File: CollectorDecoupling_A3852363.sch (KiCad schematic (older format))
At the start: 0 parts

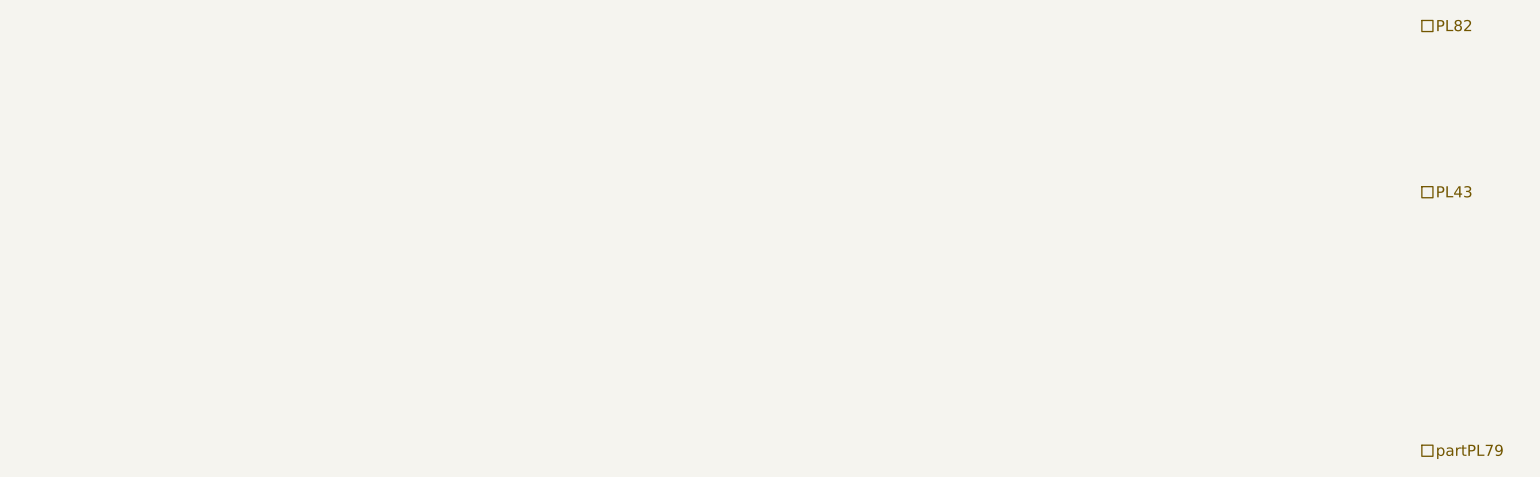
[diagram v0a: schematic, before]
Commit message: Adds Collector Decoupling (potted)
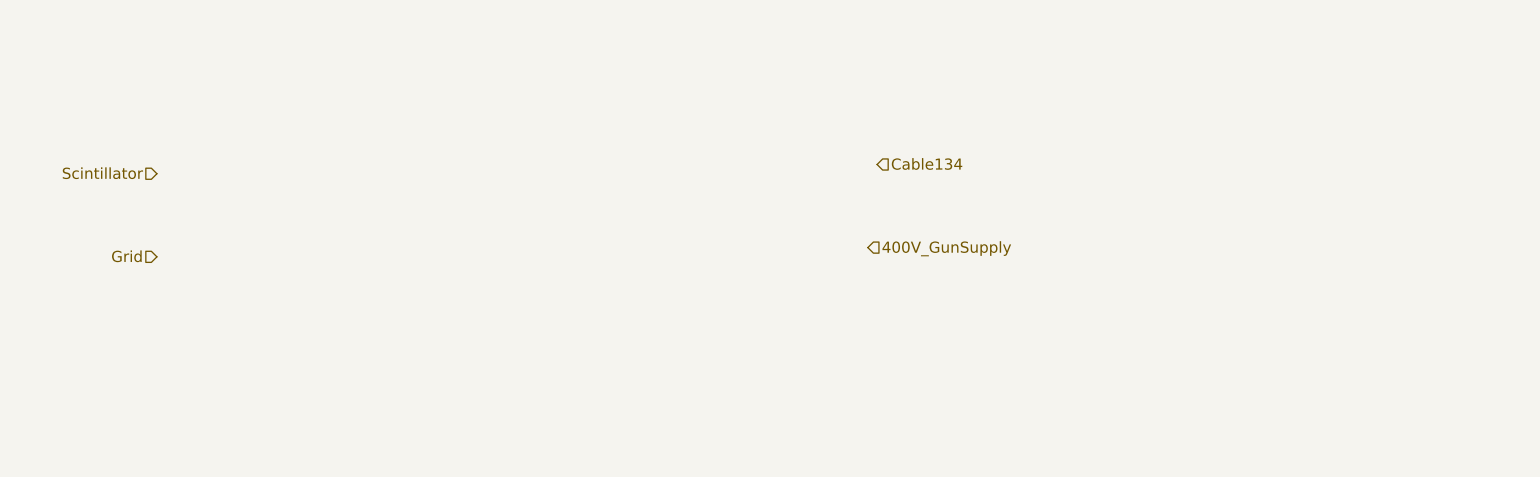
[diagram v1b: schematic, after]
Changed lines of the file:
@@
 $Descr A4 11693 8268
 encoding utf-8
-Sheet 10 15
+Sheet 15 15
 Title ""
 Date ""
@@
 Comment4 ""
 $EndDescr
-Text HLabel 8900 1600 2    60   UnSpc ~ 0
-PL82
-Text HLabel 8900 2500 2    60   UnSpc ~ 0
-PL43
-Text HLabel 8900 3900 2    60   UnSpc ~ 0
-partPL79
+Text HLabel 2050 2400 0    60   Input ~ 0
+Scintillator
+Text HLabel 2050 2850 0    60   Input ~ 0
+Grid
+Text HLabel 5950 2350 2    60   Input ~ 0
+Cable134
+Text HLabel 5900 2800 2    60   Input ~ 0
+400V_GunSupply
 $EndSCHEMATC
